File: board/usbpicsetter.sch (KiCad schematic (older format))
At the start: 10 parts, among them IC1 PIC10F200, P1 ICSP, Q1 PMOS

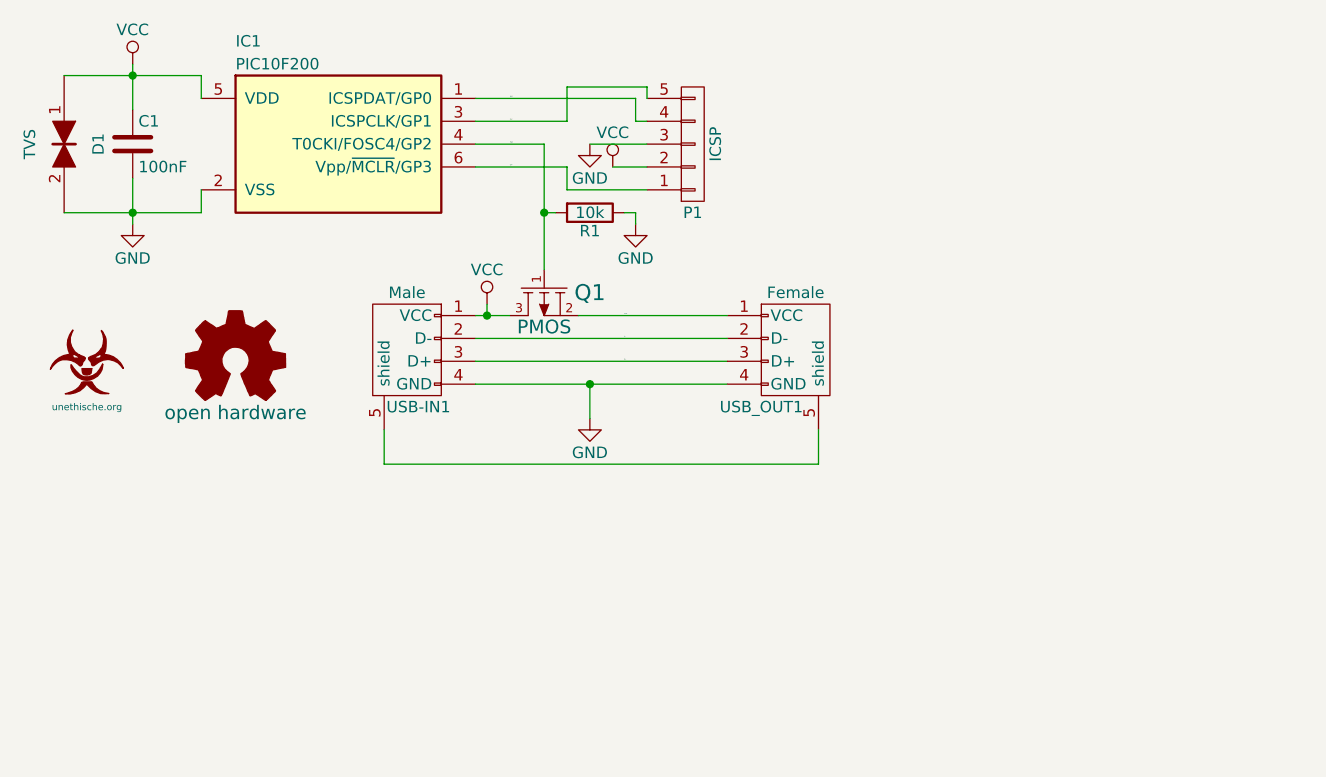
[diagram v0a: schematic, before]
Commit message: Improved silk screen, generated gerbers and modified C programm
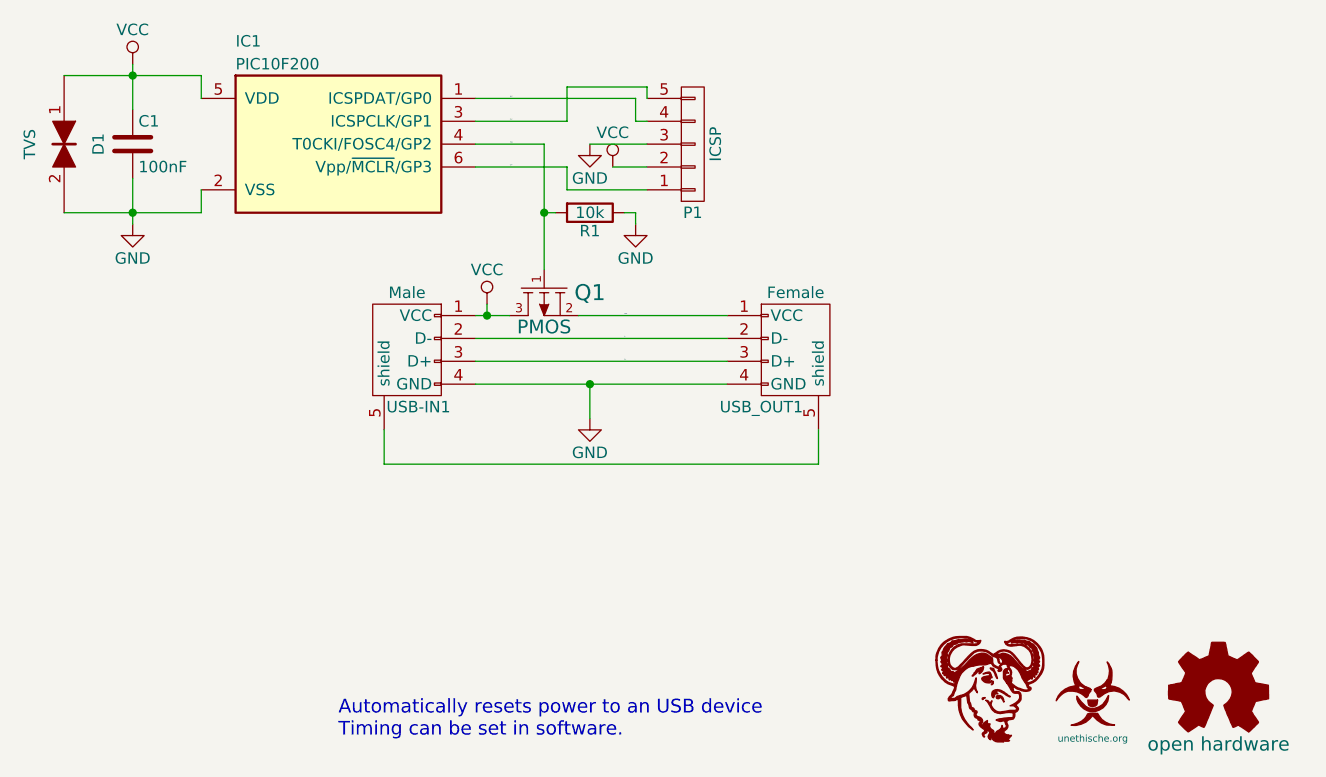
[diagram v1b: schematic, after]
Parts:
- added LO?: Gnu_GPL, symbol Gnu_GPL
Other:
- note added: "Automatically resets power to an USB device\nTiming can be set in software."
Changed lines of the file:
@@
 L OPEN_HARDWARE_1 LOGO1
 U 1 1 55A8E646
-P 3150 2950
-F 0 "LOGO1" H 3150 3225 60  0001 C CNN
-F 1 "open hardware" H 3150 2725 60  0000 C CNN
-F 2 "w_logo:Logo_silk_OSHW_6x6mm" H 3150 2950 60  0001 C CNN
-F 3 "" H 3150 2950 60  0000 C CNN
-	1    3150 2950
+P 7450 4400
+F 0 "LOGO1" H 7450 4675 60  0001 C CNN
+F 1 "open hardware" H 7450 4175 60  0000 C CNN
+F 2 "w_logo:Logo_silk_OSHW_6x6mm" H 7450 4400 60  0001 C CNN
+F 3 "" H 7450 4400 60  0000 C CNN
+	1    7450 4400
 	1    0    0    -1
 $EndComp
@@
 L unethische.org O1
 U 1 1 55A97520
-P 2500 2950
-F 0 "O1" H 2500 3150 197 0001 C CNN
-F 1 "unethische.org" H 2500 2750 30  0000 C CNN
-F 2 "jcgb:unethi_copper_silk" H 2500 2950 60  0001 C CNN
-F 3 "" H 2500 2950 60  0000 C CNN
-	1    2500 2950
+P 6900 4400
+F 0 "O1" H 6900 4600 197 0001 C CNN
+F 1 "unethische.org" H 6900 4200 30  0000 C CNN
+F 2 "jcgb:unethi_copper_silk" H 6900 4400 60  0001 C CNN
+F 3 "" H 6900 4400 60  0000 C CNN
+	1    6900 4400
 	1    0    0    -1
 $EndComp
@@
 Text Label 4350 2100 0    4    ~ 0
 VPP
+$Comp
+L Gnu_GPL LO?
+U 1 1 55BBDC0C
+P 6450 4400
+F 0 "LO?" H 6500 4750 60  0001 C CNN
+F 1 "Gnu_GPL" H 6450 4050 60  0001 C CNN
+F 2 "" H 6450 4400 60  0000 C CNN
+F 3 "" H 6450 4400 60  0000 C CNN
+	1    6450 4400
+	1    0    0    -1
+$EndComp
+Text Notes 3600 4600 0    60   ~ 0
+Automatically resets power to an USB device\nTiming can be set in software.
 $EndSCHEMATC
